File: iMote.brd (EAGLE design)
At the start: 71.6 x 60 mm, 47 parts, among them CN1 C-02235, CN2 ICSP, CN3 CC-HEADER, IC1 ATmega328P-AU, IC2 FT232RLSSOP, IC3 BLE112-A-VISUAL, Q1 16MHz, T1 2SC1815

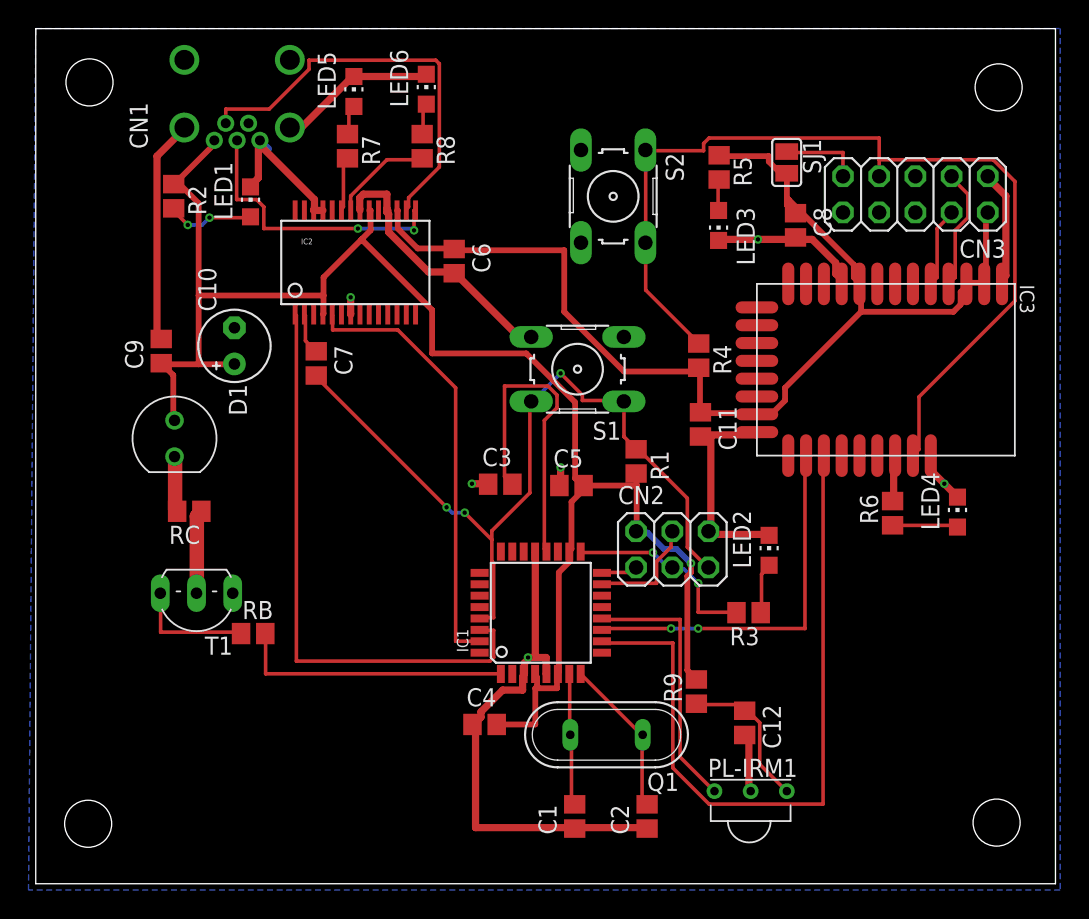
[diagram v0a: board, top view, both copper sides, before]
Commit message: avrをハンダ付けした後でも1ピンがどこにあるかわかるようにシルクに印をつけた my.lbrに移行中
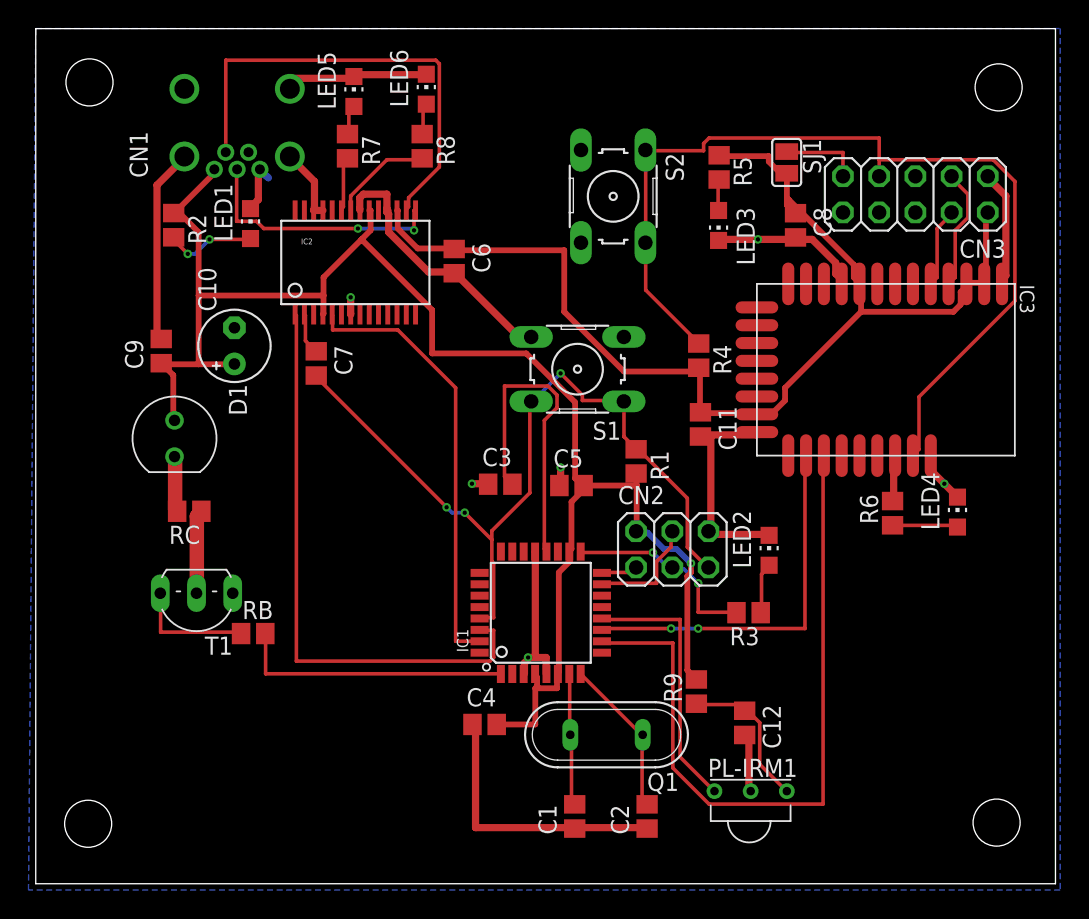
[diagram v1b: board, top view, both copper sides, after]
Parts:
- IC3: device sf-bluegiga:BLE112-A -> akizukidenshi:BLE112-A
- moved CN1 2.03 mm to (14.1, 53.5)
- moved R2 2.03 mm to (9.68, 46.2)
- moved LED1 1.52 mm to (15.1, 46.3)
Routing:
- net GND: track 140.6 -> 129.0 mm
- net USBD-: track 29.1 -> 32.8 mm
- net +5V: track 116.6 -> 114.6 mm
- net USBD+: track 19.9 -> 17.9 mm

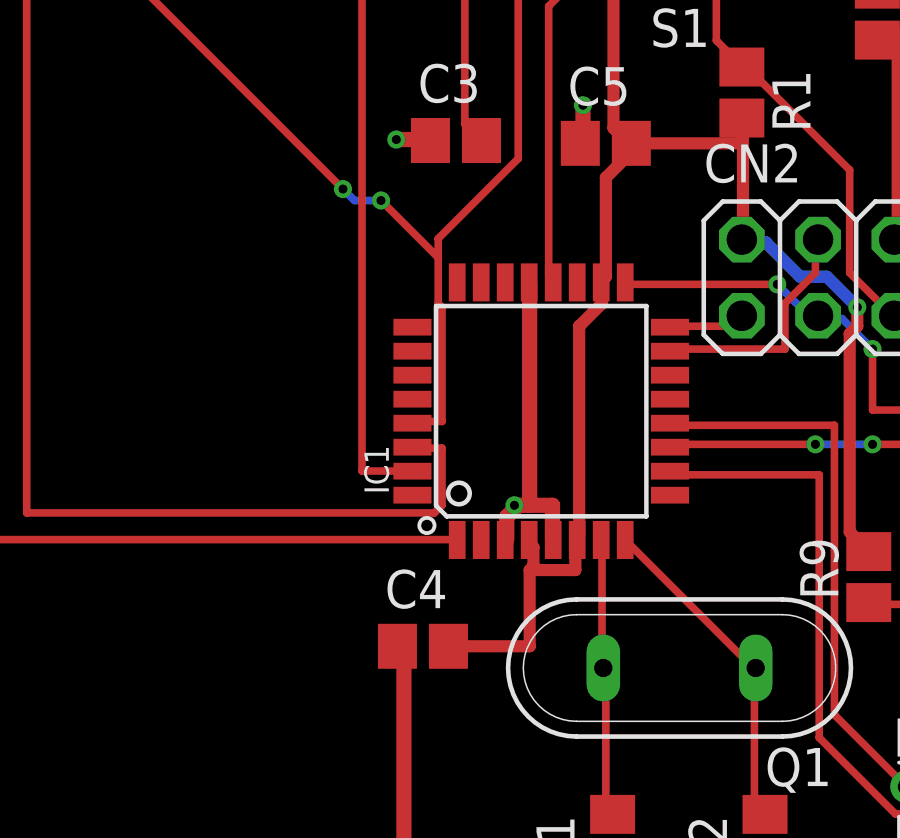
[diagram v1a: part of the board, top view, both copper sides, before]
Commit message: drillのdistanceを南里基準よりは緩くfusionpcbのdruよりは厳しいところに調整して druで警告になっているところを消した
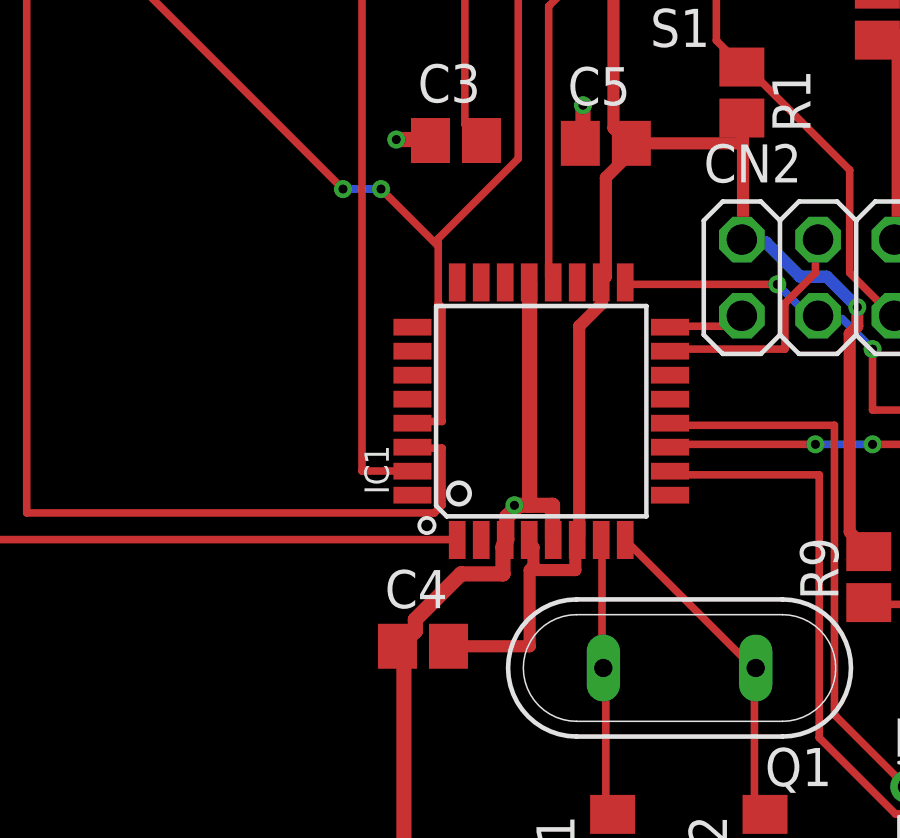
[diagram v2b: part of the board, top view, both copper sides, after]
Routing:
- net GND: track 129.0 -> 135.2 mm
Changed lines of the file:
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@@
 <setting verticaltext="up"/>
 </settings>
-<grid distance="0.1" unitdist="mm" unit="mm" style="lines" multiple="1" display="yes" altdistance="0.01" altunitdist="mm" altunit="mm"/>
+<grid distance="5" unitdist="mil" unit="mil" style="lines" multiple="1" display="yes" altdistance="1" altunitdist="mil" altunit="mil"/>
 <layers>
 <layer number="1" name="Top" color="4" fill="1" visible="yes" active="yes"/>
@@
 <param name="mnLayersViaInSmd" value="2"/>
 <param name="mdCopperDimension" value="2mm"/>
-<param name="mdDrill" value="1mm"/>
+<param name="mdDrill" value="0.5mm"/>
 <param name="mdSmdStop" value="0mil"/>
 <param name="msWidth" value="6mil"/>
@@
 <wire x1="32.131" y1="22.479" x2="32.131" y2="18.669" width="0.254" layer="1"/>
 <wire x1="32.004" y1="22.606" x2="32.131" y2="22.479" width="0.254" layer="1"/>
-<wire x1="32.004" y1="24.765" x2="32.004" y2="24.13" width="0.254" layer="1"/>
-<wire x1="32.004" y1="24.13" x2="32.004" y2="22.606" width="0.254" layer="1"/>
+<wire x1="32.004" y1="24.765" x2="32.004" y2="24.511" width="0.254" layer="1"/>
+<wire x1="32.004" y1="24.511" x2="32.004" y2="22.606" width="0.254" layer="1"/>
 <wire x1="34.671" y1="27.432" x2="32.004" y2="24.765" width="0.254" layer="1"/>
 <wire x1="34.671" y1="33.782" x2="34.671" y2="27.432" width="0.254" layer="1"/>
@@
 <wire x1="34.671" y1="33.782" x2="34.7648" y2="33.8454" width="0.254" layer="1"/>
 <wire x1="28.829" y1="26.416" x2="19.685" y2="35.56" width="0.254" layer="1"/>
-<wire x1="29.21" y1="26.035" x2="28.829" y2="26.416" width="0.254" layer="16"/>
-<wire x1="30.099" y1="26.035" x2="29.21" y2="26.035" width="0.254" layer="16"/>
-<wire x1="32.004" y1="24.13" x2="30.099" y2="26.035" width="0.254" layer="1"/>
+<wire x1="30.099" y1="26.416" x2="28.829" y2="26.416" width="0.254" layer="16"/>
+<wire x1="32.004" y1="24.511" x2="30.099" y2="26.416" width="0.254" layer="1"/>
 <wire x1="19.685" y1="35.56" x2="19.682" y2="35.66" width="0.254" layer="1"/>
 <wire x1="38.354" y1="33.909" x2="41.148" y2="33.909" width="0.254" layer="1"/>
@@
 <wire x1="34.798" y1="33.909" x2="34.7648" y2="33.8454" width="0.254" layer="16"/>
 <via x="28.829" y="26.416" extent="1-16" drill="0.3"/>
-<via x="30.099" y="26.035" extent="1-16" drill="0.3"/>
+<via x="30.099" y="26.416" extent="1-16" drill="0.3"/>
 <via x="36.83" y="35.814" extent="1-16" drill="0.3"/>
 </signal>
@@
 <contactref element="IC1" pad="21"/>
 <contactref element="C5" pad="1"/>
+<contactref element="C4" pad="1"/>
+<contactref element="IC1" pad="5"/>
+<contactref element="IC1" pad="3"/>
 <wire x1="42.799" y1="3.937" x2="37.846" y2="3.937" width="0.508" layer="1"/>
 <wire x1="37.846" y1="3.937" x2="37.818" y2="3.872" width="0.508" layer="1"/>
@@
 <wire x1="35.052" y1="15.875" x2="34.671" y2="15.875" width="0.508" layer="1"/>
 <wire x1="35.814" y1="14.732" x2="35.814" y2="15.875" width="0.508" layer="1"/>
+<wire x1="34.29" y1="14.732" x2="34.238" y2="14.7194" width="0.508" layer="1"/>
+<wire x1="35.814" y1="14.732" x2="35.838" y2="14.7194" width="0.508" layer="1"/>
 <wire x1="35.052" y1="15.875" x2="35.052" y2="23.241" width="0.508" layer="1"/>
 <wire x1="35.052" y1="23.241" x2="35.038" y2="23.3046" width="0.508" layer="1"/>
+<wire x1="31.242" y1="11.684" x2="30.734" y2="11.176" width="0.508" layer="1"/>
+<wire x1="31.242" y1="12.065" x2="31.242" y2="11.684" width="0.508" layer="1"/>
+<wire x1="32.766" y1="13.589" x2="31.242" y2="12.065" width="0.508" layer="1"/>
+<wire x1="34.163" y1="13.589" x2="32.766" y2="13.589" width="0.508" layer="1"/>
+<wire x1="34.163" y1="14.478" x2="34.163" y2="13.589" width="0.508" layer="1"/>
+<wire x1="30.734" y1="11.176" x2="30.646" y2="11.176" width="0.508" layer="1"/>
+<wire x1="34.163" y1="14.478" x2="34.238" y2="14.7194" width="0.508" layer="1"/>
 <wire x1="30.861" y1="3.937" x2="37.592" y2="3.937" width="0.508" layer="1"/>
 <wire x1="30.861" y1="11.049" x2="30.861" y2="3.937" width="0.508" layer="1"/>
 <wire x1="37.592" y1="3.937" x2="37.818" y2="3.872" width="0.508" layer="1"/>
+<wire x1="30.861" y1="11.049" x2="30.646" y2="11.176" width="0.508" layer="1"/>
 <wire x1="56.515" y1="42.164" x2="56.552" y2="42.09" width="0.508" layer="1"/>
 <wire x1="53.213" y1="45.212" x2="50.673" y2="45.212" width="0.508" layer="1"/>
@@
 <via x="50.673" y="45.212" extent="1-16" drill="0.3"/>
 <via x="34.544" y="15.875" extent="1-16" drill="0.3"/>
-<contactref element="C4" pad="1"/>
-<contactref element="IC1" pad="5"/>
-<contactref element="IC1" pad="3"/>
-<wire x1="35.814" y1="14.732" x2="35.838" y2="14.7194" width="0" layer="19" extent="1-1"/>
-<wire x1="34.238" y1="14.7194" x2="34.29" y2="14.732" width="0" layer="19" extent="1-1"/>
-<wire x1="30.861" y1="11.049" x2="34.238" y2="14.7194" width="0" layer="19" extent="1-1"/>
-<wire x1="30.646" y1="11.176" x2="30.861" y2="11.049" width="0" layer="19" extent="1-1"/>
 </signal>
 <signal name="N$10">

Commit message: 全部品my.lbr化中
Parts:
- C1, C11, C12, C2, C3, C4, C5, C6, C7, C8, C9: device rcl:C2012 -> my:2012
- CN1: device akizukidenshi:C-02235 -> my:C-02235
- D1: device akizukidenshi:LED -> my:LED
- IC1: device Arduino-AVR:TQFP32-08 -> my:TQFP32-08
- IC2: device akizukidenshi:SSOP28DB -> my:SSOP28DB
- IC3: device akizukidenshi:BLE112-A -> my:BLE112-A
- LED1: device led:CHIP-LED0805 -> led:CHIPLED_0805
- PL-IRM1: device akizukidenshi:IR-RECEIVER -> my:IR-RECEIVER
- R1, R2, R3, R4, R5, R6, R7, R8, R9, RB, RC: device resistor:R2012 -> my:2012
- moved CN3 24.7 mm to (37.2, 44.9)
- moved LED4 24.4 mm to (46.7, 9.58)
- moved R6 24.4 mm to (42.1, 9.50)
- moved IC3 24.1 mm to (38.0, 25.5)
- moved PL-IRM1 22.5 mm to (27.7, 5.50)
- moved STANDOFF3 22.4 mm to (47.0, 47.0)
- moved C2 21.9 mm to (21.1, 3.35)
- moved C1 21.9 mm to (16.0, 3.35)
- moved Q1 21.7 mm to (18.5, 7.45)
- moved C12 21.2 mm to (28.8, 8.26), turned to 180 degrees
- moved R4 21.0 mm to (45.5, 16.1)
- moved STANDOFF1 20.5 mm to (47.0, 3.01)
- moved R3 18.9 mm to (33.3, 10.3)
- moved LED2 18.8 mm to (35.6, 13.3)
- moved C4 17.5 mm to (14.0, 10.7)
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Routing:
- net GND: track 135.2 -> 0.00 mm, vias 6 -> 0
- net +5V: track 114.6 -> 0.00 mm, vias 1 -> 0
- net +3V3: track 81.7 -> 0.00 mm
- net !BLE/RST: track 67.2 -> 0.00 mm
- net !RESET: track 57.1 -> 0.00 mm, vias 3 -> 0
- net D6/BLERX: track 49.9 -> 0.00 mm
- net D0/USBRX: track 41.2 -> 0.00 mm
- net USBD-: track 32.8 -> 0.00 mm
- net D1/USBTX: track 30.9 -> 0.00 mm
- net D7/BLETX: track 26.5 -> 0.00 mm, vias 2 -> 0
- net AREF: track 22.5 -> 0.00 mm
- net D3/IROUT: track 19.3 -> 0.00 mm
- net D8/IRIN: track 18.6 -> 0.00 mm
- net USBD+: track 17.9 -> 0.00 mm, vias 2 -> 0
- net D13/SCK: track 13.9 -> 0.00 mm, vias 2 -> 0
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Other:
- board size 71.6 x 60 mm -> 50 x 50 mm

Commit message: 全部品my.lbr化中
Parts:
- D1: device my:LED -> my:LED-3MM
- LED1: device led:CHIPLED_0805 -> my:LED-2012
- LED2, LED3, LED4, LED5, LED6: device led:CHIP-LED0805 -> my:LED-2012
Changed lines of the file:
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@@
 <element name="C9" library="my" package="2012" value="0.1uF" x="7.736" y="33.514"/>
 <element name="C10" library="rcl" package="E2,5-5" value="10uF" x="12.442" y="29.742" rot="R90"/>
-<element name="LED1" library="led" package="CHIPLED_0805" value="5V" x="11.57" y="38.822"/>
-<element name="LED2" library="led" package="CHIP-LED0805" value="ICSP" x="35.588" y="13.336"/>
+<element name="LED1" library="my" package="LED-2012" value="5V" x="11.57" y="38.822"/>
+<element name="LED2" library="my" package="LED-2012" value="ICSP" x="35.588" y="13.336"/>
 <element name="T1" library="transistor" package="TO92-ECB" value="2SC1815" x="6.78" y="18.386" rot="R180"/>
 <element name="RB" library="my" package="2012" value="4.7k" x="5.258" y="14.054"/>
@@
 </element>
 <element name="R5" library="my" package="2012" value="330" x="40.45" y="39.764" rot="R270"/>
-<element name="LED3" library="led" package="CHIP-LED0805" value="3.3V" x="39.412" y="36.19" rot="R180"/>
+<element name="LED3" library="my" package="LED-2012" value="3.3V" x="39.412" y="36.19" rot="R180"/>
 <element name="R6" library="my" package="2012" value="330" x="42.122" y="9.502" rot="R90"/>
-<element name="LED4" library="led" package="CHIP-LED0805" value="BLE" x="46.676" y="9.578"/>
+<element name="LED4" library="my" package="LED-2012" value="BLE" x="46.676" y="9.578"/>
 <element name="CN3" library="pinhead" package="2X05" value="CC-HEADER" x="37.222" y="44.872" rot="R180"/>
 <element name="SJ1" library="jumper" package="SJ" value="0" x="44.692" y="37.612" rot="R270"/>
@@
 <element name="R9" library="my" package="2012" value="200" x="33.456" y="6.302" rot="R90"/>
 <element name="C12" library="my" package="2012" value="4.7uF" x="28.788" y="8.256" rot="R180"/>
-<element name="D1" library="my" package="LED" value="OSIR5113A" x="6.798" y="28.192" rot="R270"/>
+<element name="D1" library="my" package="LED-3MM" value="OSIR5113A" x="6.798" y="28.192" rot="R270"/>
 <element name="IC2" library="my" package="SSOP28DB" value="FT232RLSSOP" x="18.926" y="36.094">
 <attribute name="PROD_ID" value="IC-00870" x="18.926" y="36.094" size="1.778" layer="27" display="off"/>
@@
 <element name="C7" library="my" package="2012" value="0.1uF" x="16.182" y="29.51" rot="R270"/>
 <element name="R7" library="my" package="2012" value="680" x="18.874" y="41.25" rot="R270"/>
-<element name="LED5" library="led" package="CHIP-LED0805" value="USB/TX" x="18.824" y="45.59"/>
+<element name="LED5" library="my" package="LED-2012" value="USB/TX" x="18.824" y="45.59"/>
 <element name="R8" library="my" package="2012" value="680" x="24.114" y="41.25" rot="R270"/>
-<element name="LED6" library="led" package="CHIP-LED0805" value="USB/RX" x="24.124" y="45.67"/>
+<element name="LED6" library="my" package="LED-2012" value="USB/RX" x="24.124" y="45.67"/>
 <element name="U$1" library="git-revision" package="GIT-REVISION" value="ccb4477" x="0.254" y="-3.048"/>
 <element name="STANDOFF3" library="SparkFun-Electromechanical" package="STAND-OFF" value="STAND-OFF" x="47.004" y="47.01"/>
@@
 <contactref element="R2" pad="2"/>
 <contactref element="LED1" pad="A"/>
-<wire x1="6.68" y1="37.26" x2="11.57" y2="37.772" width="0" layer="19" extent="1-1"/>
+<wire x1="6.68" y1="37.26" x2="10.62" y2="38.822" width="0" layer="19" extent="1-1"/>
 </signal>
 <signal name="N$2">
@@
 <contactref element="R3" pad="1"/>
 <contactref element="LED2" pad="A"/>
-<wire x1="34.24" y1="10.282" x2="35.588" y2="12.286" width="0" layer="19" extent="1-1"/>
+<wire x1="34.24" y1="10.282" x2="34.638" y2="13.336" width="0" layer="19" extent="1-1"/>
 </signal>
 <signal name="N$1">
@@
 <wire x1="44.812" y1="35.25" x2="42.302" y2="46.142" width="0" layer="19" extent="1-1"/>
 <wire x1="46.152" y1="31.56" x2="44.812" y2="35.25" width="0" layer="19" extent="1-1"/>
-<wire x1="39.412" y1="35.14" x2="44.812" y2="35.25" width="0" layer="19" extent="1-1"/>
-<wire x1="34.902" y1="31.56" x2="39.412" y2="35.14" width="0" layer="19" extent="1-1"/>
+<wire x1="38.462" y1="36.19" x2="44.812" y2="35.25" width="0" layer="19" extent="1-1"/>
+<wire x1="34.902" y1="31.56" x2="38.462" y2="36.19" width="0" layer="19" extent="1-1"/>
 <wire x1="30.2574" y1="34.4808" x2="34.902" y2="31.56" width="0" layer="19" extent="1-1"/>
 <wire x1="27.7672" y1="36.3666" x2="30.2574" y2="34.4808" width="0" layer="19" extent="1-1"/>
@@
 <wire x1="15.19" y1="41.508" x2="16.001" y2="39.75" width="0" layer="19" extent="1-1"/>
 <wire x1="13.09" y1="40.608" x2="15.19" y2="41.508" width="0" layer="19" extent="1-1"/>
-<wire x1="11.57" y1="39.872" x2="13.09" y2="40.608" width="0" layer="19" extent="1-1"/>
-<wire x1="7.79" y1="41.508" x2="11.57" y2="39.872" width="0" layer="19" extent="1-1"/>
+<wire x1="12.52" y1="38.822" x2="13.09" y2="40.608" width="0" layer="19" extent="1-1"/>
+<wire x1="7.79" y1="41.508" x2="12.52" y2="38.822" width="0" layer="19" extent="1-1"/>
 <wire x1="15.19" y1="46.258" x2="15.19" y2="41.508" width="0" layer="19" extent="1-1"/>
-<wire x1="18.824" y1="46.64" x2="15.19" y2="46.258" width="0" layer="19" extent="1-1"/>
+<wire x1="19.774" y1="45.59" x2="15.19" y2="46.258" width="0" layer="19" extent="1-1"/>
 <wire x1="7.79" y1="46.258" x2="7.79" y2="41.508" width="0" layer="19" extent="1-1"/>
 <wire x1="18.601" y1="32.438" x2="21.2648" y2="36.3666" width="0" layer="19" extent="1-1"/>
 <wire x1="30.2574" y1="40.9832" x2="27.7672" y2="36.3666" width="0" layer="19" extent="1-1"/>
-<wire x1="24.124" y1="46.72" x2="18.824" y2="46.64" width="0" layer="19" extent="1-1"/>
+<wire x1="25.074" y1="45.67" x2="19.774" y2="45.59" width="0" layer="19" extent="1-1"/>
 <wire x1="12.442" y1="31.012" x2="18.601" y2="32.438" width="0" layer="19" extent="1-1"/>
 <wire x1="8.686" y1="33.514" x2="12.442" y2="31.012" width="0" layer="19" extent="1-1"/>
@@
 <wire x1="28.952" y1="21.16" x2="22.922" y2="25.53" width="0" layer="19" extent="1-1"/>
 <wire x1="32.706" y1="15.232" x2="28.952" y2="21.16" width="0" layer="19" extent="1-1"/>
-<wire x1="35.588" y1="14.386" x2="32.706" y2="15.232" width="0" layer="19" extent="1-1"/>
-<wire x1="41.642" y1="15.28" x2="35.588" y2="14.386" width="0" layer="19" extent="1-1"/>
+<wire x1="36.538" y1="13.336" x2="32.706" y2="15.232" width="0" layer="19" extent="1-1"/>
+<wire x1="41.642" y1="15.28" x2="36.538" y2="13.336" width="0" layer="19" extent="1-1"/>
 <wire x1="41.152" y1="19.51" x2="41.642" y2="15.28" width="0" layer="19" extent="1-1"/>
-<wire x1="46.676" y1="10.628" x2="41.642" y2="15.28" width="0" layer="19" extent="1-1"/>
+<wire x1="47.626" y1="9.578" x2="41.642" y2="15.28" width="0" layer="19" extent="1-1"/>
 <wire x1="27.838" y1="8.256" x2="32.706" y2="15.232" width="0" layer="19" extent="1-1"/>
 <wire x1="27.664" y1="5.498" x2="27.838" y2="8.256" width="0" layer="19" extent="1-1"/>
@@
 <contactref element="R5" pad="2"/>
 <contactref element="LED3" pad="A"/>
-<wire x1="39.412" y1="37.24" x2="40.45" y2="38.814" width="0" layer="19" extent="1-1"/>
+<wire x1="40.362" y1="36.19" x2="40.45" y2="38.814" width="0" layer="19" extent="1-1"/>
 </signal>
 <signal name="BLE/P0_0" class="3">
@@
 <contactref element="R6" pad="1"/>
 <contactref element="LED4" pad="A"/>
-<wire x1="42.122" y1="8.552" x2="46.676" y2="8.528" width="0" layer="19" extent="1-1"/>
+<wire x1="42.122" y1="8.552" x2="45.726" y2="9.578" width="0" layer="19" extent="1-1"/>
 </signal>
 <signal name="BLE/P2_2">
@@
 <contactref element="R7" pad="1"/>
 <contactref element="LED5" pad="A"/>
-<wire x1="18.874" y1="42.2" x2="18.824" y2="44.54" width="0" layer="19" extent="1-1"/>
+<wire x1="18.874" y1="42.2" x2="17.874" y2="45.59" width="0" layer="19" extent="1-1"/>
 </signal>
 <signal name="N$6">
 <contactref element="R8" pad="1"/>
 <contactref element="LED6" pad="A"/>
-<wire x1="24.114" y1="42.2" x2="24.124" y2="44.62" width="0" layer="19" extent="1-1"/>
+<wire x1="24.114" y1="42.2" x2="23.174" y2="45.67" width="0" layer="19" extent="1-1"/>
 </signal>
 <signal name="D8/IRIN">
